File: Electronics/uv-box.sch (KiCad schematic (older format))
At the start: 73 parts, among them P1 CONN_2

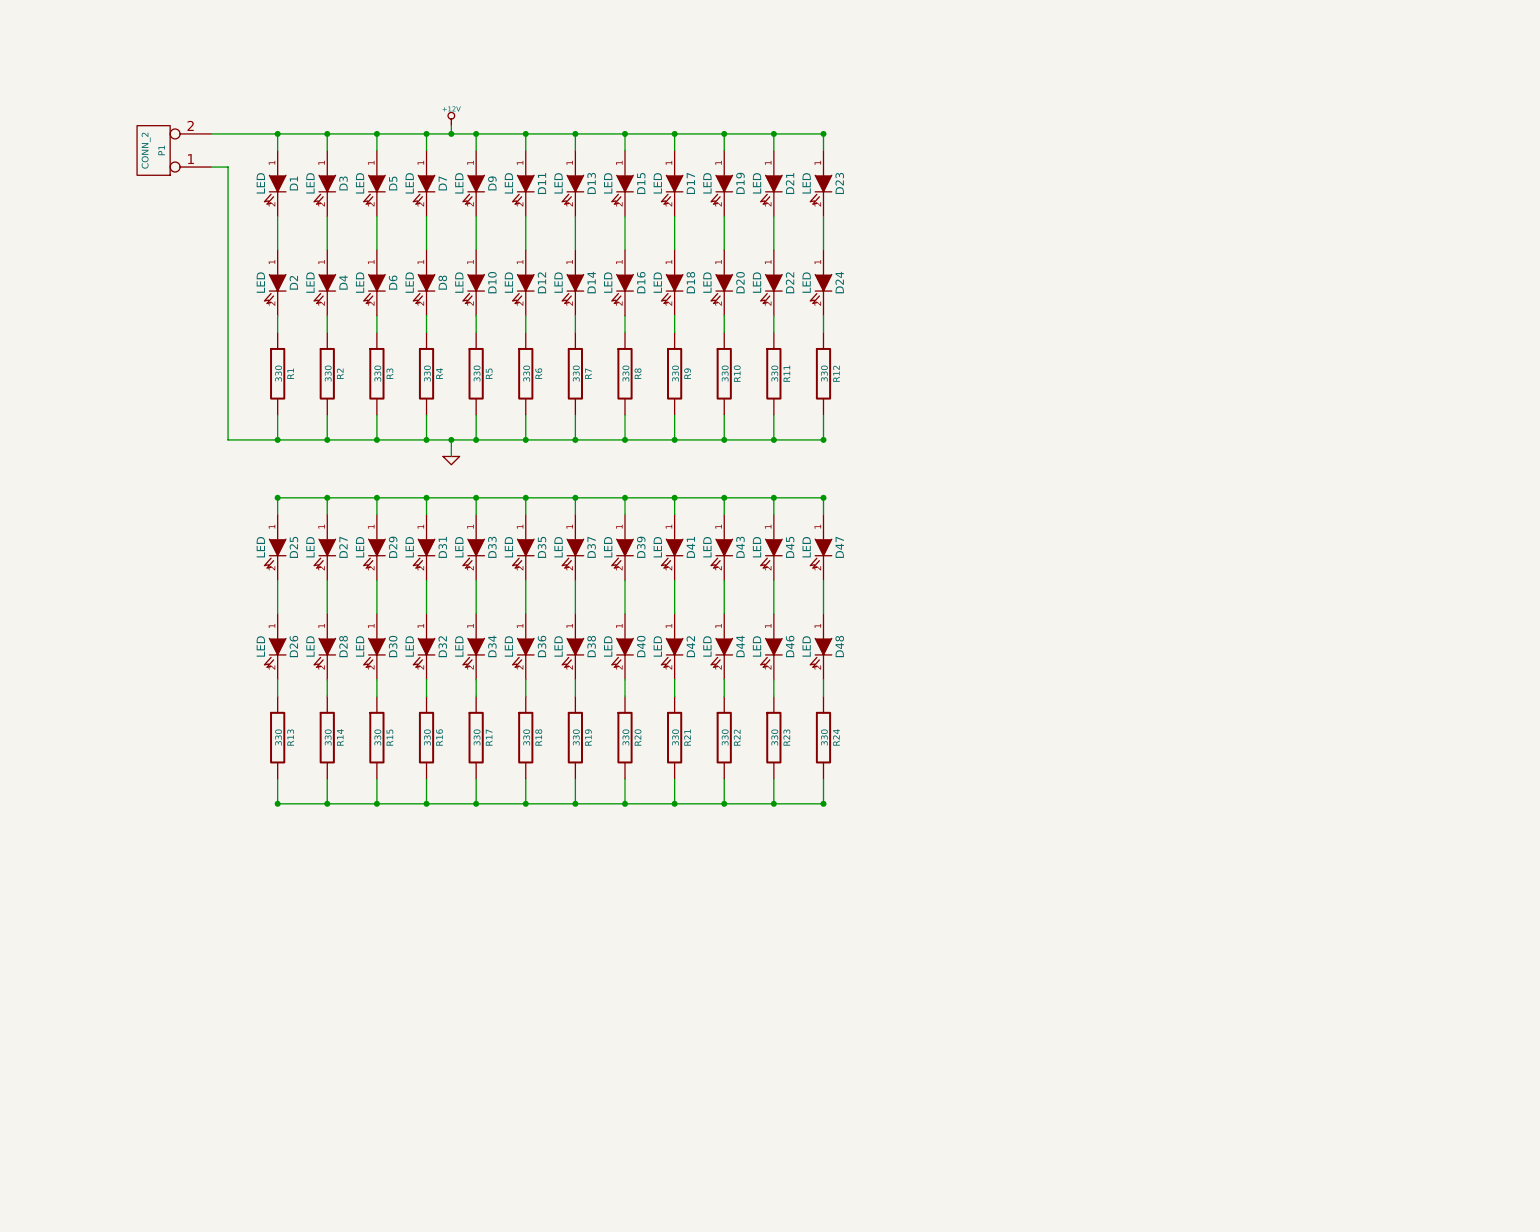
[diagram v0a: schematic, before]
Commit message: 84 LED per panel.
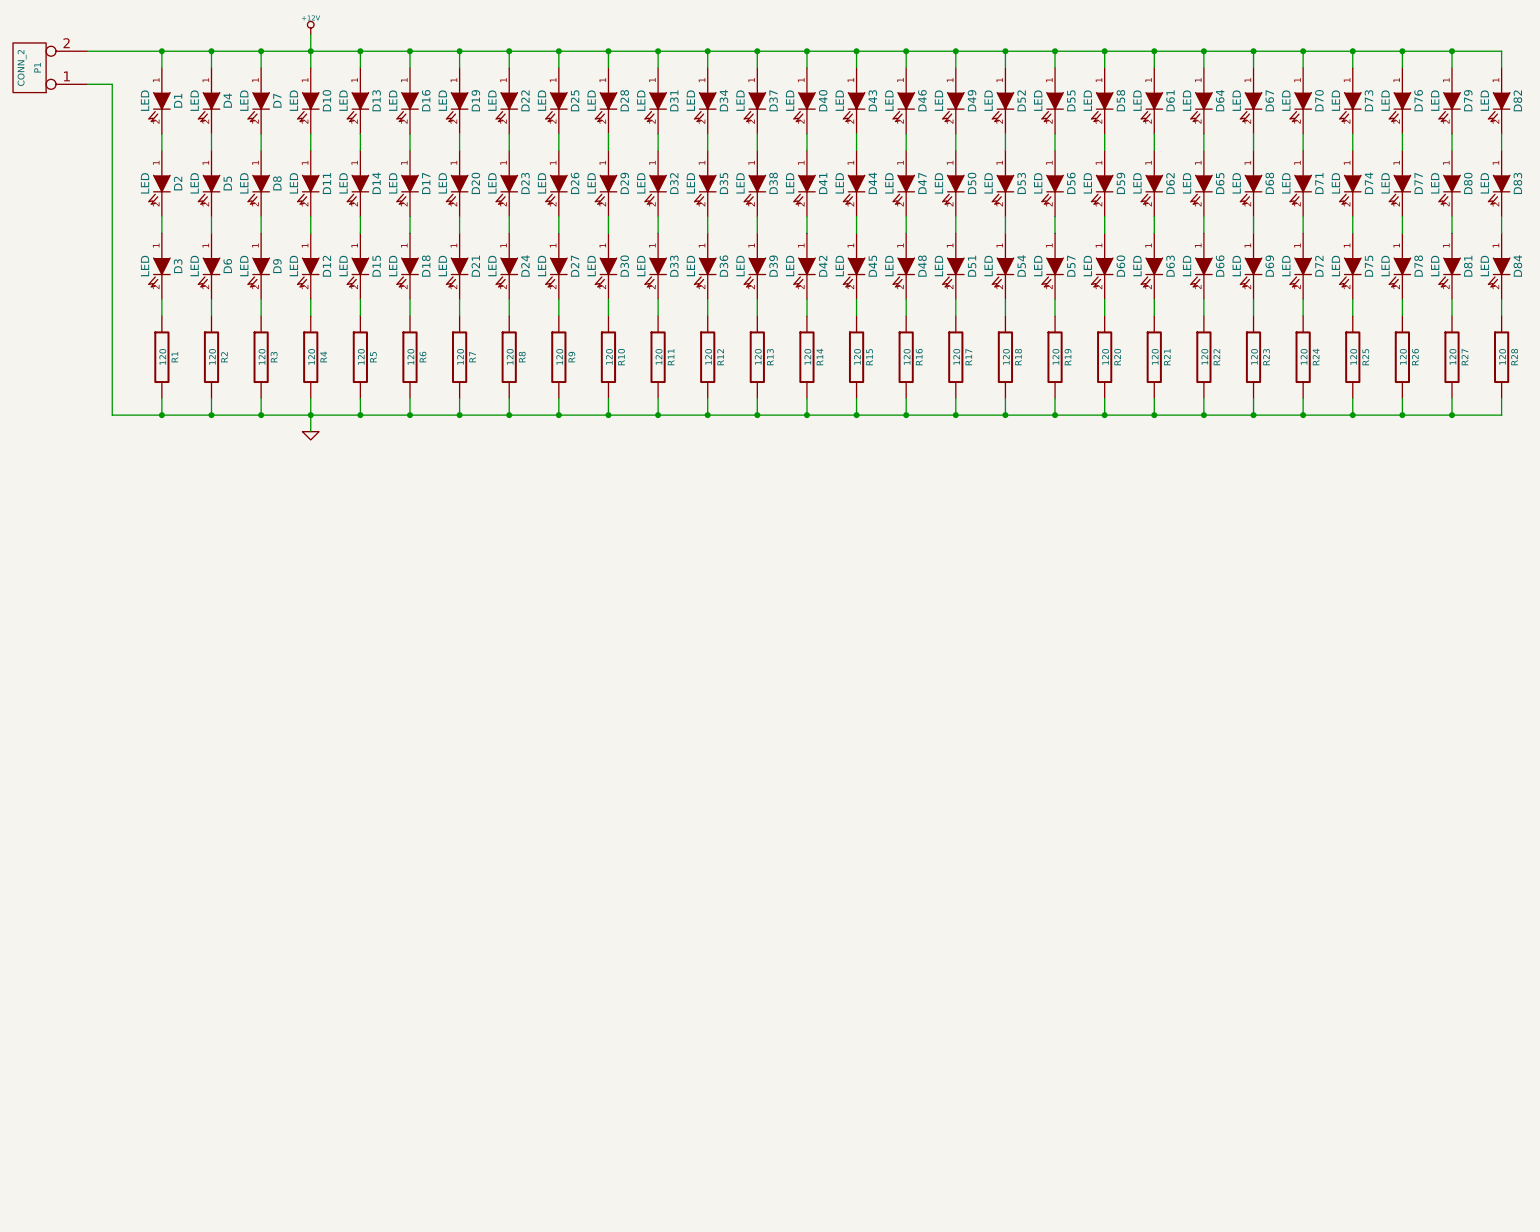
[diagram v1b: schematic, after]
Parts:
- removed D10, D11: LED, ~, symbol LED
- added D49, D50, D51, D52, D53, D54, D55, D56, D57, D58, D59, D60, D61, D62, D63, D64, D65, D66, D67, D68, D69, D7, D70, D71, D72, D73, D74, D75, D76, D77, D78, D79, D8, D80, D81, D82, D83, D84: LED, ~, symbol LED
- added R25, R26, R27, R28: 120, ~, symbol R
- R1, R10, R11, R12, R13, R14, R15, R16, R17, R18, R19, R2, R20, R21, R22, R23, R24, R3, R4, R5, R6, R7, R8, R9: value 330 -> 120
- renumbered D7 to D10, D8 to D11
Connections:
- net +12V: now also D16.1 (A), D22.1 (A), D25.1 (A), D28.1 (A), D31.1 (A), D34.1 (A), D37.1 (A), D4.1 (A), D40.1 (A), D43.1 (A), D46.1 (A), D49.1 (A), D52.1 (A), D55.1 (A), D58.1 (A), D61.1 (A), D64.1 (A), D67.1 (A), D7.1 (A), D70.1 (A), D73.1 (A), D76.1 (A), D79.1 (A), D82.1 (A); no longer D15.1 (A), D17.1 (A), D21.1 (A), D23.1 (A), D3.1 (A), D5.1 (A), D9.1 (A)
- net GND: now also R13.2, R14.2, R15.2, R16.2, R17.2, R18.2, R19.2, R20.2, R21.2, R22.2, R23.2, R24.2, R25.2, R26.2, R27.2, R28.2
- net at D3.2 (K): now also R1.1; no longer D4.1 (A)
- net at D9.2 (K): now also R3.1
- net at D12.1 (A): now also D11.2 (K)
- net at D15.2 (K): now also R5.1; no longer D16.1 (A)
- net at D21.2 (K): now also R7.1; no longer D22.1 (A)
- net at D2.2 (K): now also D3.1 (A); no longer R1.1
- net at D4.2 (K): now also D5.1 (A); no longer R2.1
- net at D6.2 (K): now also R2.1; no longer R3.1
- net at R4.1: now also D12.2 (K); no longer D11.2 (K)
- net at R6.1: now also D18.2 (K); no longer D12.2 (K)
- net at D14.2 (K): now also D15.1 (A); no longer R7.1
- net at D16.2 (K): now also D17.1 (A); no longer R8.1
- net at R9.1: now also D27.2 (K); no longer D18.2 (K)
- net at D20.2 (K): now also D21.1 (A); no longer R10.1
- net at R11.1: now also D33.2 (K); no longer D22.2 (K)
- net at D24.2 (K): now also R8.1; no longer R12.1
- net at D39.2 (K): now also R13.1; no longer D40.1 (A)
- net at D45.2 (K): now also R15.1; no longer D46.1 (A)
- net at D26.2 (K): now also D27.1 (A); no longer R13.1
- net at D28.2 (K): now also D29.1 (A); no longer R14.1
- net at D30.2 (K): now also R10.1; no longer R15.1
- net at D32.2 (K): now also D33.1 (A); no longer R16.1
- net at D34.2 (K): now also D35.1 (A); no longer R17.1
- net at D36.2 (K): now also R12.1; no longer R18.1
- net at D38.2 (K): now also D39.1 (A); no longer R19.1
- net at D40.2 (K): now also D41.1 (A); no longer R20.1
- net at D42.2 (K): now also R14.1; no longer R21.1
- net at D44.2 (K): now also D45.1 (A); no longer R22.1
- net at D46.2 (K): now also D47.1 (A); no longer R23.1
- net at D48.2 (K): now also R16.1; no longer R24.1
- new net: D7.2 (K), D8.1 (A)
- new net: D8.2 (K), D9.1 (A)
- new net: D22.2 (K), D23.1 (A)
- new net: D52.2 (K), D53.1 (A)
- new net: D53.2 (K), D54.1 (A)
- new net: D54.2 (K), R18.1
- new net: D49.2 (K), D50.1 (A)
- new net: D50.2 (K), D51.1 (A)
- new net: D51.2 (K), R17.1
- new net: D61.2 (K), D62.1 (A)
- new net: D62.2 (K), D63.1 (A)
- new net: D63.2 (K), R21.1
- new net: D58.2 (K), D59.1 (A)
- new net: D59.2 (K), D60.1 (A)
- new net: D60.2 (K), R20.1
- new net: D55.2 (K), D56.1 (A)
- new net: D56.2 (K), D57.1 (A)
- new net: D57.2 (K), R19.1
- new net: D73.2 (K), D74.1 (A)
- new net: D74.2 (K), D75.1 (A)
- new net: D75.2 (K), R25.1
- new net: D70.2 (K), D71.1 (A)
- new net: D71.2 (K), D72.1 (A)
- new net: D72.2 (K), R24.1
- new net: D67.2 (K), D68.1 (A)
- new net: D68.2 (K), D69.1 (A)
- new net: D69.2 (K), R23.1
- new net: D64.2 (K), D65.1 (A)
- new net: D65.2 (K), D66.1 (A)
- new net: D66.2 (K), R22.1
- new net: D82.2 (K), D83.1 (A)
- new net: D83.2 (K), D84.1 (A)
- new net: D84.2 (K), R28.1
- new net: D79.2 (K), D80.1 (A)
- new net: D80.2 (K), D81.1 (A)
- new net: D81.2 (K), R27.1
- new net: D76.2 (K), D77.1 (A)
- new net: D77.2 (K), D78.1 (A)
- new net: D78.2 (K), R26.1
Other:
- moved on the sheet: D10, D11, P1, R4

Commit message: Add second panel, and controller.
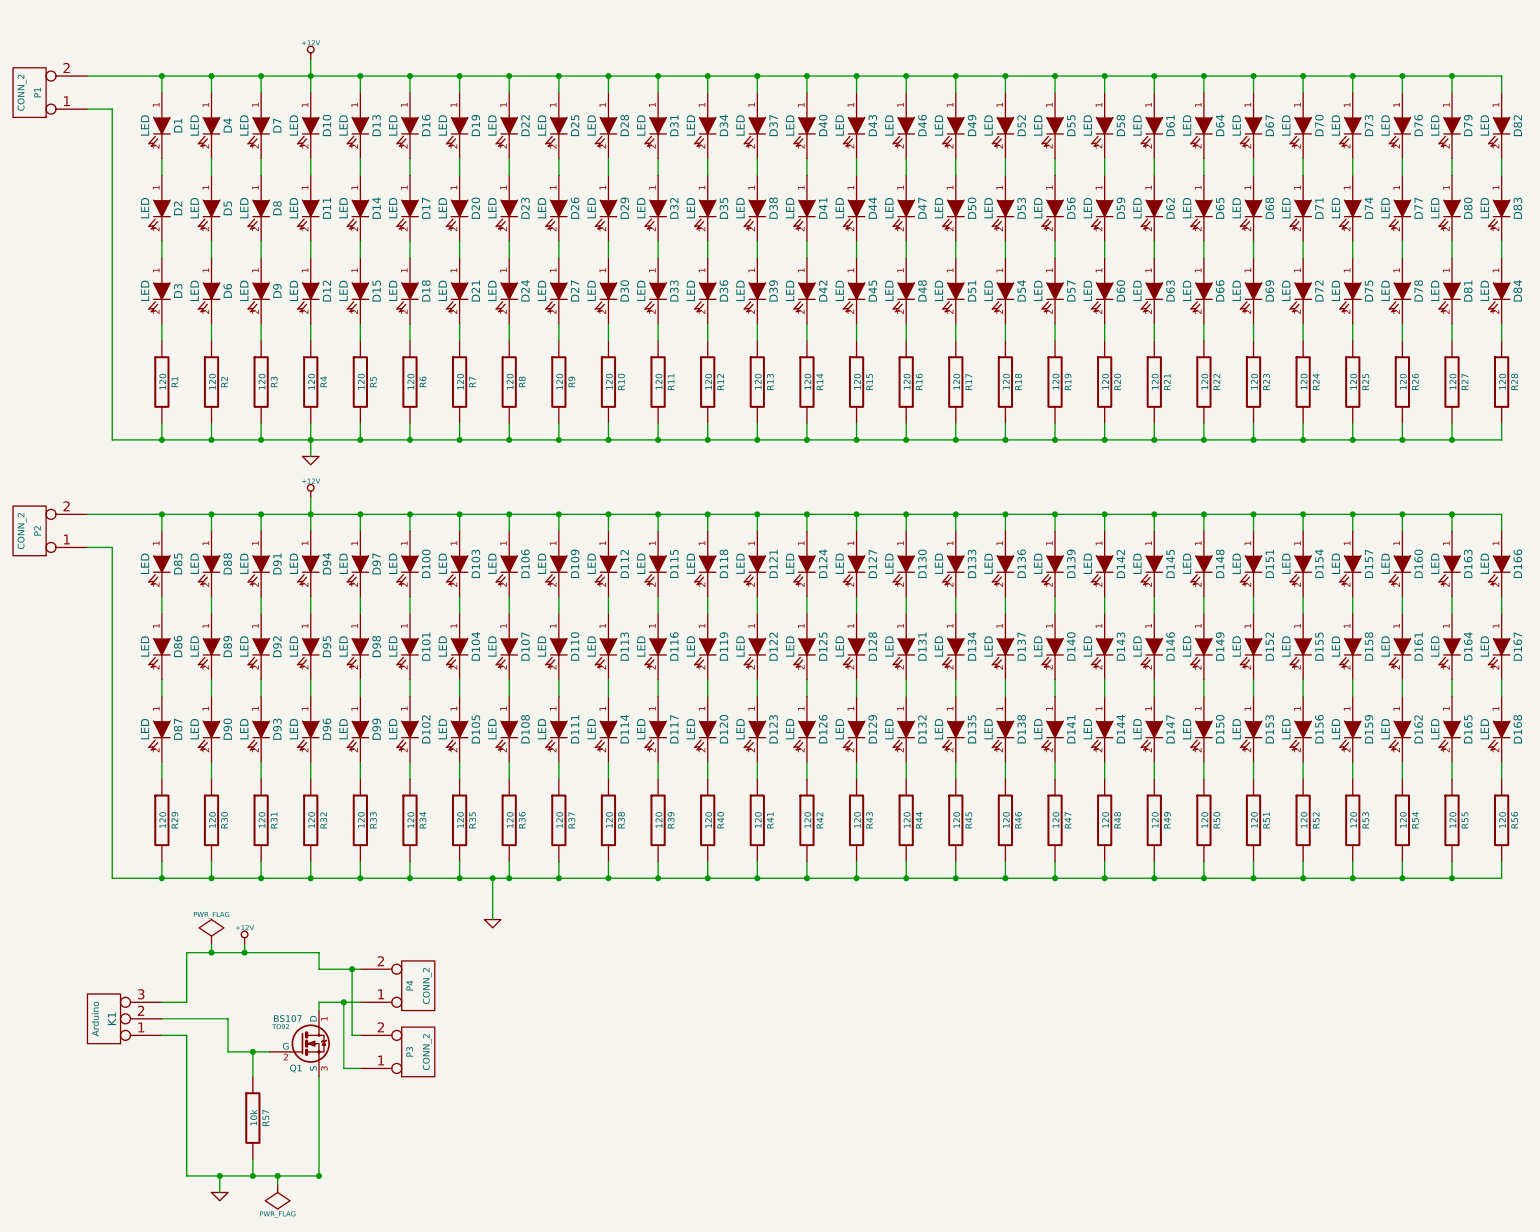
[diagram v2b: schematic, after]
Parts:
- added D100, D101, D102, D103, D104, D105, D106, D107, D108, D109, D110, D111, D112, D113, D114, D115, D116, D117, D118, D119, D120, D121, D122, D123, D124, D125, D126, D127, D128, D129, D130, D131, D132, D133, D134, D135, D136, D137, D138, D139, D140, D141, D142, D143, D144, D145, D146, D147, D148, D149, D150, D151, D152, D153, D154, D155, D156, D157, D158, D159, D160, D161, D162, D163, D164, D165, D166, D167, D168, D85, D86, D87, D88, D89, D90, D91, D92, D93, D94, D95, D96, D97, D98, D99: LED, ~, symbol LED
- added K1: Arduino, symbol CONN_3
- added P2, P3, P4: CONN_2, symbol CONN_2
- added Q1: BS107, TO92, symbol BS107
- added R29, R30, R31, R32, R33, R34, R35, R36, R37, R38, R39, R40, R41, R42, R43, R44, R45, R46, R47, R48, R49, R50, R51, R52, R53, R54, R55, R56: 120, ~, symbol R
- added R57: 10k, ~, symbol R
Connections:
- net +12V: now also D100.1 (A), D103.1 (A), D106.1 (A), D109.1 (A), D112.1 (A), D115.1 (A), D118.1 (A), D121.1 (A), D124.1 (A), D127.1 (A), D130.1 (A), D133.1 (A), D136.1 (A), D139.1 (A), D142.1 (A), D145.1 (A), D148.1 (A), D151.1 (A), D154.1 (A), D157.1 (A), D160.1 (A), D163.1 (A), D166.1 (A), D85.1 (A), D88.1 (A), D91.1 (A), D94.1 (A), D97.1 (A), K1.3 (P3), P2.2 (PM), P3.2 (PM), P4.2 (PM)
- net GND: now also K1.1 (P1), P2.1 (P1), Q1.3 (S), R29.2, R30.2, R31.2, R32.2, R33.2, R34.2, R35.2, R36.2, R37.2, R38.2, R39.2, R40.2, R41.2, R42.2, R43.2, R44.2, R45.2, R46.2, R47.2, R48.2, R49.2, R50.2, R51.2, R52.2, R53.2, R54.2, R55.2, R56.2, R57.2
- new net: D94.2 (K), D95.1 (A)
- new net: D95.2 (K), D96.1 (A)
- new net: D96.2 (K), R32.1
- new net: D91.2 (K), D92.1 (A)
- new net: D92.2 (K), D93.1 (A)
- new net: D93.2 (K), R31.1
- new net: D88.2 (K), D89.1 (A)
- new net: D89.2 (K), D90.1 (A)
- new net: D90.2 (K), R30.1
- new net: D85.2 (K), D86.1 (A)
- new net: D86.2 (K), D87.1 (A)
- new net: D87.2 (K), R29.1
- new net: D103.2 (K), D104.1 (A)
- new net: D104.2 (K), D105.1 (A)
- new net: D105.2 (K), R35.1
- new net: D100.2 (K), D101.1 (A)
- new net: D101.2 (K), D102.1 (A)
- new net: D102.2 (K), R34.1
- new net: D97.2 (K), D98.1 (A)
- new net: D98.2 (K), D99.1 (A)
- new net: D99.2 (K), R33.1
- new net: D115.2 (K), D116.1 (A)
- new net: D116.2 (K), D117.1 (A)
- new net: D117.2 (K), R39.1
- new net: D112.2 (K), D113.1 (A)
- new net: D113.2 (K), D114.1 (A)
- new net: D114.2 (K), R38.1
- new net: D109.2 (K), D110.1 (A)
- new net: D110.2 (K), D111.1 (A)
- new net: D111.2 (K), R37.1
- new net: D106.2 (K), D107.1 (A)
- new net: D107.2 (K), D108.1 (A)
- new net: D108.2 (K), R36.1
- new net: D124.2 (K), D125.1 (A)
- new net: D125.2 (K), D126.1 (A)
- new net: D126.2 (K), R42.1
- new net: D121.2 (K), D122.1 (A)
- new net: D122.2 (K), D123.1 (A)
- new net: D123.2 (K), R41.1
- new net: D118.2 (K), D119.1 (A)
- new net: D119.2 (K), D120.1 (A)
- new net: D120.2 (K), R40.1
- new net: D136.2 (K), D137.1 (A)
- new net: D137.2 (K), D138.1 (A)
- new net: D138.2 (K), R46.1
- new net: D133.2 (K), D134.1 (A)
- new net: D134.2 (K), D135.1 (A)
- new net: D135.2 (K), R45.1
- new net: D130.2 (K), D131.1 (A)
- new net: D131.2 (K), D132.1 (A)
- new net: D132.2 (K), R44.1
- new net: D127.2 (K), D128.1 (A)
- new net: D128.2 (K), D129.1 (A)
- new net: D129.2 (K), R43.1
- new net: D145.2 (K), D146.1 (A)
- new net: D146.2 (K), D147.1 (A)
- new net: D147.2 (K), R49.1
- new net: D142.2 (K), D143.1 (A)
- new net: D143.2 (K), D144.1 (A)
- new net: D144.2 (K), R48.1
- new net: D139.2 (K), D140.1 (A)
- new net: D140.2 (K), D141.1 (A)
- new net: D141.2 (K), R47.1
- new net: D157.2 (K), D158.1 (A)
- new net: D158.2 (K), D159.1 (A)
- new net: D159.2 (K), R53.1
- new net: D154.2 (K), D155.1 (A)
- new net: D155.2 (K), D156.1 (A)
- new net: D156.2 (K), R52.1
- new net: D151.2 (K), D152.1 (A)
- new net: D152.2 (K), D153.1 (A)
- new net: D153.2 (K), R51.1
- new net: D148.2 (K), D149.1 (A)
- new net: D149.2 (K), D150.1 (A)
- new net: D150.2 (K), R50.1
- new net: D166.2 (K), D167.1 (A)
- new net: D167.2 (K), D168.1 (A)
- new net: D168.2 (K), R56.1
- new net: D163.2 (K), D164.1 (A)
- new net: D164.2 (K), D165.1 (A)
- new net: D165.2 (K), R55.1
- new net: D160.2 (K), D161.1 (A)
- new net: D161.2 (K), D162.1 (A)
- new net: D162.2 (K), R54.1
- new net: P3.1 (P1), P4.1 (P1), Q1.1 (D)
- new net: K1.2 (PM), Q1.2 (G), R57.1
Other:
- moved on the sheet: D1, D10, D11, D12, D13, D14, D15, D16, D17, D18, D19, D2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
